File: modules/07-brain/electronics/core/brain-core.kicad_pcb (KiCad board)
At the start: 2 copper layers, 60.5 x 110 mm, 104 parts, among them J1 Conn_02x03_Odd_Even, J10 Conn_01x02, J11 Conn_01x01, J13 Conn_01x03, J2 Conn_02x02_Odd_Even, J3 Conn_02x02_Odd_Even, J4 Conn_02x03_Odd_Even, J5 Conn_01x02, J6 Conn_02x05_Odd_Even, J7 Conn_02x05_Odd_Even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

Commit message: Verfied JLCPCB for Brain 1.0
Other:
- board text added: "SHMØERGH MODULEUR"
- board text added: "SM-07 BRAIN V1.0 / 2025 DEC"
- board text removed: "HM-07 Brain V0.1 / 2025 Sept"
- board text removed: "SHMØERGH HOG MODULEUR"

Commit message: Changed Brain J_DEV header to horizontal
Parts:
- removed the G*** at (133.7, 116.0)
- J_DEV1: footprint Connector_PinHeader_2.54mm:PinHeader_1x02_P2.54mm_Vertical -> Connector_PinHeader_2.54mm:PinHeader_1x02_P2.54mm_Horizontal
- moved J_DEV1 2.54 mm to (133.8, 60.5), turned to 90 degrees
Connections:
- J_DEV1 pad 1: /MCU/UART_TX -> /MCU/UART_RX
- J_DEV1 pad 2: /MCU/UART_RX -> /MCU/UART_TX

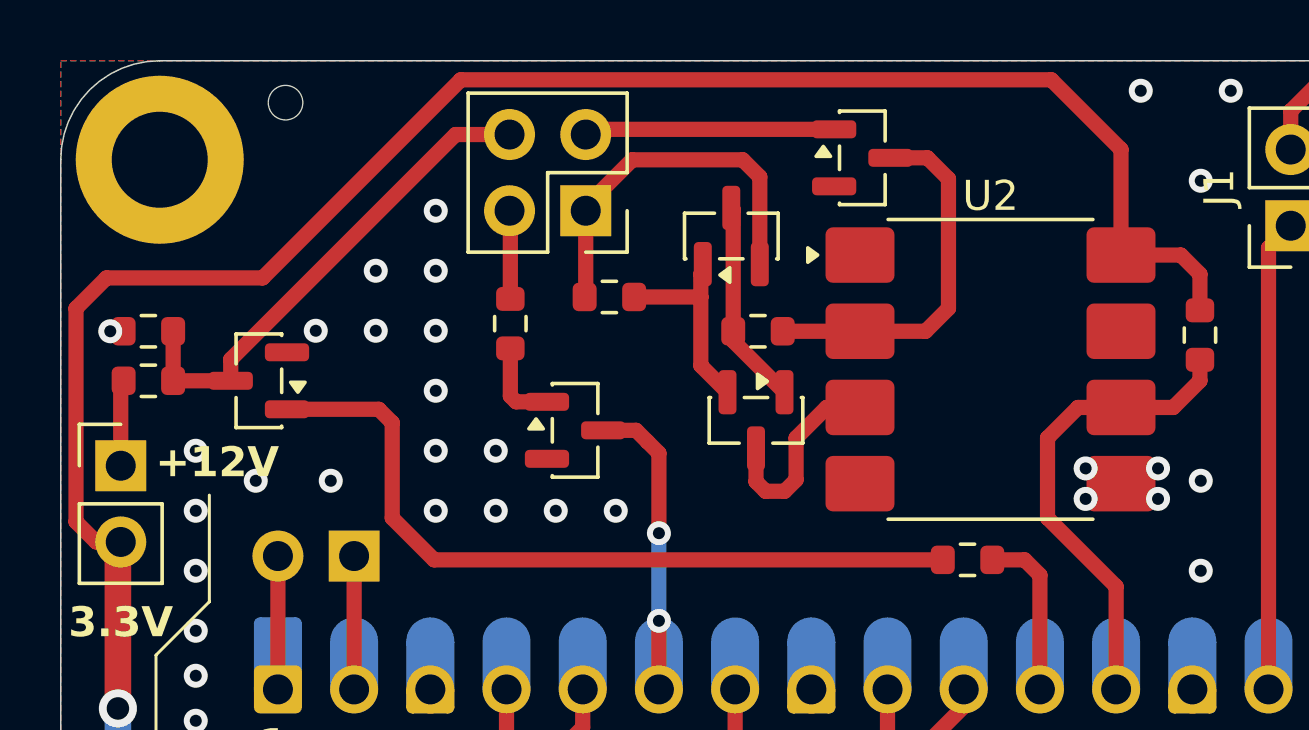
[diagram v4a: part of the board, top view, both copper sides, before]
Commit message: Added protection resistor to pulse out on Brain
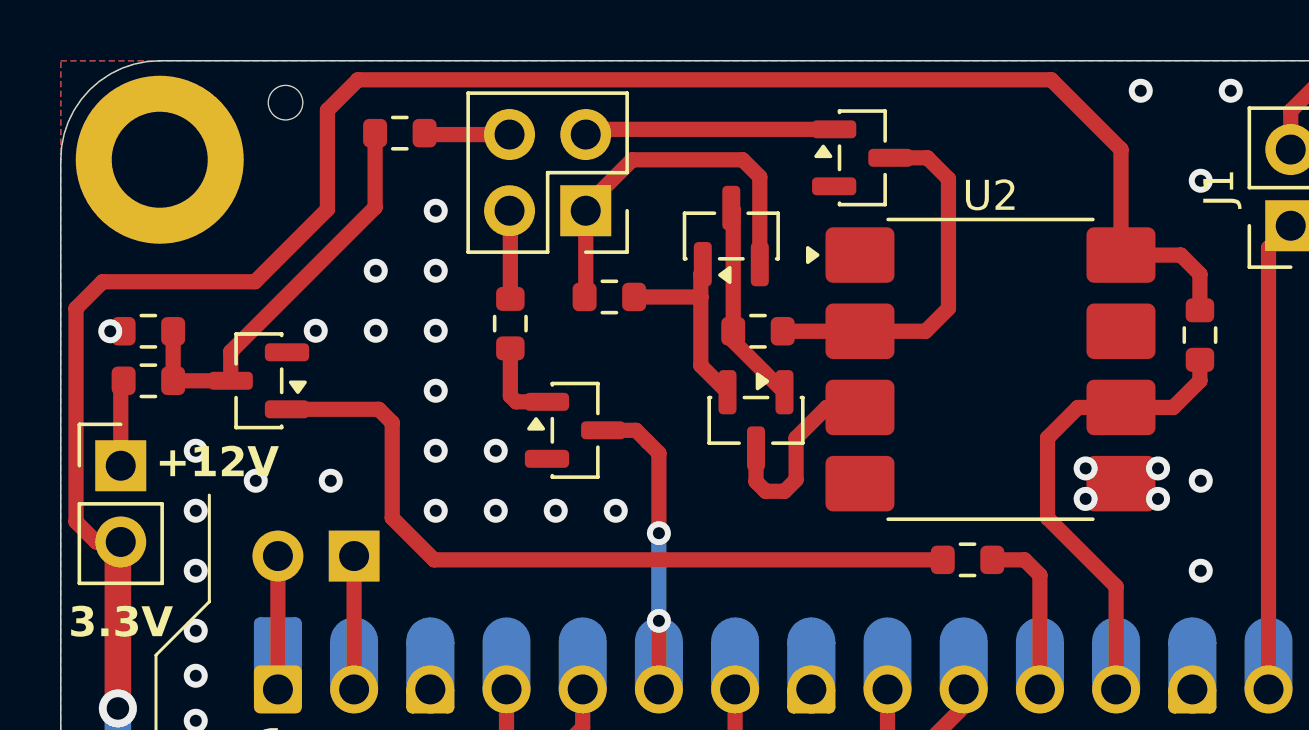
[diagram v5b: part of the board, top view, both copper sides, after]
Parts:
- added R13: 1k, Resistor_SMD:R_0603_1608Metric, F.Cu at (135.3, 46.4)
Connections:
- Q3 pad 3: PULSE_OUT -> Net-(Q3-C)
- R3 pad 1: PULSE_OUT -> Net-(Q3-C)
- R4 pad 2: PULSE_OUT -> Net-(Q3-C)
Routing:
- net PULSE_OUT: track 16.7 -> 2.85 mm
- net Net-(Q3-C): track 0.00 -> 13.8 mm
- net +3.3V: track 155.3 -> 157.2 mm

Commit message: KiCAD version update - Brain
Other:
- board text added: "SM-07 BRAIN V1.1"
- board text removed: "SM-07 BRAIN V1.0 / 2025 DEC"
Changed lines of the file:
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@@
 		)
 	)
-	(gr_text "SM-07 \nBRAIN\nV1.0 / 2025 DEC"
+	(gr_text "SM-07 \nBRAIN\nV1.1"
 		(at 148.384 122.354 0)
 		(layer "B.SilkS")
@@
 			(justify left bottom mirror)
 		)
-		(render_cache "SM-07 \nBRAIN\nV1.0 / 2025 DEC" 0
+		(render_cache "SM-07 \nBRAIN\nV1.1" 0
 			(polygon
 				(pts
@@
 			(polygon
 				(pts
-					(xy 145.167089 121.129498) (xy 145.167089 122.012161) (xy 145.016257 122.012161) (xy 145.016257 121.719415)
-					(xy 144.869849 121.719415) (xy 144.869849 121.568583) (xy 145.016257 121.568583) (xy 145.016257 121.129498)
-				)
-			)
-			(polygon
-				(pts
-					(xy 145.020751 122.007667) (xy 145.020751 122.1585) (xy 144.577172 122.1585) (xy 144.577172 122.007667)
-				)
-			)
-			(polygon
-				(pts
-					(xy 145.020751 120.98309) (xy 145.020751 121.133992) (xy 144.577172 121.133992) (xy 144.577172 120.98309)
-				)
-			)
-			(polygon
-				(pts
-					(xy 144.581667 121.129498) (xy 144.581667 121.275836) (xy 144.728005 121.275836) (xy 144.728005 121.426739)
-					(xy 144.581667 121.426739) (xy 144.581667 122.012161) (xy 144.430764 122.012161) (xy 144.430764 121.129498)
-				)
-			)
-			(polygon
-				(pts
-					(xy 144.874343 121.422245) (xy 144.874343 121.573077) (xy 144.723511 121.573077) (xy 144.723511 121.422245)
-				)
-			)
-			(polygon
-				(pts
-					(xy 142.680956 121.129498) (xy 142.680956 121.426739) (xy 142.530124 121.426739) (xy 142.530124 121.129498)
-				)
-			)
-			(polygon
-				(pts
-					(xy 143.120041 122.007667) (xy 143.120041 122.304908) (xy 142.969209 122.304908) (xy 142.969209 122.007667)
-				)
-			)
-			(polygon
-				(pts
-					(xy 142.973703 121.714921) (xy 142.973703 122.012161) (xy 142.822801 122.012161) (xy 142.822801 121.714921)
-				)
-			)
-			(polygon
-				(pts
-					(xy 142.827295 121.422245) (xy 142.827295 121.719415) (xy 142.676462 121.719415) (xy 142.676462 121.422245)
-				)
-			)
-			(polygon
-				(pts
-					(xy 142.534618 120.836752) (xy 142.534618 121.133992) (xy 142.383716 121.133992) (xy 142.383716 120.836752)
-				)
-			)
-			(polygon
-				(pts
-					(xy 141.072993 121.861329) (xy 141.072993 122.1585) (xy 140.336668 122.1585) (xy 140.336668 122.007667)
-					(xy 140.922161 122.007667) (xy 140.922161 121.861329)
-				)
-			)
-			(polygon
-				(pts
-					(xy 140.483076 121.133992) (xy 140.483076 120.98309) (xy 140.926655 120.98309) (xy 140.926655 121.133992)
-				)
-			)
-			(polygon
-				(pts
-					(xy 140.48757 121.129498) (xy 140.48757 121.426739) (xy 140.336668 121.426739) (xy 140.336668 121.129498)
-				)
-			)
-			(polygon
-				(pts
-					(xy 140.926655 121.714921) (xy 140.926655 121.865823) (xy 140.775752 121.865823) (xy 140.775752 121.714921)
-				)
-			)
-			(polygon
-				(pts
-					(xy 141.072993 121.129498) (xy 141.072993 121.28033) (xy 140.922161 121.28033) (xy 140.922161 121.129498)
-				)
-			)
-			(polygon
-				(pts
-					(xy 140.633908 121.422245) (xy 140.633908 121.573077) (xy 140.483076 121.573077) (xy 140.483076 121.422245)
-				)
-			)
-			(polygon
-				(pts
-					(xy 140.780246 121.568583) (xy 140.780246 121.719415) (xy 140.629414 121.719415) (xy 140.629414 121.568583)
-				)
-			)
-			(polygon
-				(pts
-					(xy 140.049469 121.129498) (xy 140.049469 122.012161) (xy 139.898637 122.012161) (xy 139.898637 121.719415)
-					(xy 139.752228 121.719415) (xy 139.752228 121.568583) (xy 139.898637 121.568583) (xy 139.898637 121.129498)
-				)
-			)
-			(polygon
-				(pts
-					(xy 139.903131 122.007667) (xy 139.903131 122.1585) (xy 139.459552 122.1585) (xy 139.459552 122.007667)
-				)
-			)
-			(polygon
-				(pts
-					(xy 139.903131 120.98309) (xy 139.903131 121.133992) (xy 139.459552 121.133992) (xy 139.459552 120.98309)
-				)
-			)
-			(polygon
-				(pts
-					(xy 139.464046 121.129498) (xy 139.464046 121.275836) (xy 139.610384 121.275836) (xy 139.610384 121.426739)
-					(xy 139.464046 121.426739) (xy 139.464046 122.012161) (xy 139.313144 122.012161) (xy 139.313144 121.129498)
-				)
-			)
-			(polygon
-				(pts
-					(xy 139.756722 121.422245) (xy 139.756722 121.573077) (xy 139.60589 121.573077) (xy 139.60589 121.422245)
-				)
-			)
-			(polygon
-				(pts
-					(xy 139.025945 121.861329) (xy 139.025945 122.1585) (xy 138.28962 122.1585) (xy 138.28962 122.007667)
-					(xy 138.875113 122.007667) (xy 138.875113 121.861329)
-				)
-			)
-			(polygon
-				(pts
-					(xy 138.436028 121.133992) (xy 138.436028 120.98309) (xy 138.879607 120.98309) (xy 138.879607 121.133992)
-				)
-			)
-			(polygon
-				(pts
-					(xy 138.440522 121.129498) (xy 138.440522 121.426739) (xy 138.28962 121.426739) (xy 138.28962 121.129498)
-				)
-			)
-			(polygon
-				(pts
-					(xy 138.879607 121.714921) (xy 138.879607 121.865823) (xy 138.728704 121.865823) (xy 138.728704 121.714921)
-				)
-			)
-			(polygon
-				(pts
-					(xy 139.025945 121.129498) (xy 139.025945 121.28033) (xy 138.875113 121.28033) (xy 138.875113 121.129498)
-				)
-			)
-			(polygon
-				(pts
-					(xy 138.58686 121.422245) (xy 138.58686 121.573077) (xy 138.436028 121.573077) (xy 138.436028 121.422245)
-				)
-			)
-			(polygon
-				(pts
-					(xy 138.733198 121.568583) (xy 138.733198 121.719415) (xy 138.582366 121.719415) (xy 138.582366 121.568583)
-				)
-			)
-			(polygon
-				(pts
-					(xy 138.002421 120.98309) (xy 138.002421 121.573077) (xy 137.412504 121.573077) (xy 137.412504 121.422245)
-					(xy 137.851588 121.422245) (xy 137.851588 121.133992) (xy 137.266096 121.133992) (xy 137.266096 120.98309)
-				)
-			)
-			(polygon
-				(pts
-					(xy 137.416998 121.568583) (xy 137.416998 122.012161) (xy 137.266096 122.012161) (xy 137.266096 121.568583)
-				)
-			)
-			(polygon
-				(pts
-					(xy 137.412504 122.007667) (xy 137.856083 122.007667) (xy 137.856083 122.1585) (xy 137.412504 122.1585)
-				)
-			)
-			(polygon
-				(pts
-					(xy 137.851588 122.012161) (xy 137.851588 121.861329) (xy 138.002421 121.861329) (xy 138.002421 122.012161)
-				)
-			)
-			(polygon
-				(pts
-					(xy 135.955372 120.98309) (xy 135.955372 122.1585) (xy 135.365456 122.1585) (xy 135.365456 122.007667)
-					(xy 135.80454 122.007667) (xy 135.80454 121.133992) (xy 135.365456 121.133992) (xy 135.365456 120.98309)
-				)
-			)
-			(polygon
-				(pts
-					(xy 135.36995 121.129498) (xy 135.36995 122.012161) (xy 135.219047 122.012161) (xy 135.219047 121.129498)
-				)
-			)
-			(polygon
-				(pts
-					(xy 134.931848 120.98309) (xy 134.931848 122.1585) (xy 134.195523 122.1585) (xy 134.195523 122.007667)
-					(xy 134.781016 122.007667) (xy 134.781016 121.573077) (xy 134.341932 121.573077) (xy 134.341932 121.422245)
-					(xy 134.781016 121.422245) (xy 134.781016 121.133992) (xy 134.195523 121.133992) (xy 134.195523 120.98309)
-				)
-			)
-			(polygon
-				(pts
-					(xy 133.908324 121.129498) (xy 133.908324 122.012161) (xy 133.757492 122.012161) (xy 133.757492 121.129498)
-				)
-			)
-			(polygon
-				(pts
-					(xy 133.761986 122.007667) (xy 133.761986 122.1585) (xy 133.318408 122.1585) (xy 133.318408 122.007667)
-				)
-			)
-			(polygon
-				(pts
-					(xy 133.322902 121.861329) (xy 133.322902 122.012161) (xy 133.171999 122.012161) (xy 133.171999 121.861329)
-				)
-			)
-			(polygon
-				(pts
-					(xy 133.761986 120.98309) (xy 133.761986 121.133992) (xy 133.318408 121.133992) (xy 133.318408 120.98309)
-				)
-			)
-			(polygon
-				(pts
-					(xy 133.322902 121.129498) (xy 133.322902 121.28033) (xy 133.171999 121.28033) (xy 133.171999 121.129498)
-				)
-			)
+					(xy 144.874343 121.28033) (xy 144.874343 122.007667) (xy 145.167089 122.007667) (xy 145.167089 122.1585)
+					(xy 144.430764 122.1585) (xy 144.430764 122.007667) (xy 144.723511 122.007667) (xy 144.723511 120.98309)
+					(xy 144.874343 120.98309) (xy 144.874343 121.129498) (xy 145.167089 121.129498) (xy 145.167089 121.28033)
+				)
+			)

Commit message: Updated rev. number in Brain
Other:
- board text added: "SM-07 BRAIN V1.2"
- board text removed: "SM-07 BRAIN V1.1"
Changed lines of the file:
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@@
 		)
 	)
-	(gr_text "SM-07 \nBRAIN\nV1.1"
+	(gr_text "SM-07 \nBRAIN\nV1.2"
 		(at 148.384 122.354 0)
 		(layer "B.SilkS")
@@
 			(justify left bottom mirror)
 		)
-		(render_cache "SM-07 \nBRAIN\nV1.1" 0
+		(render_cache "SM-07 \nBRAIN\nV1.2" 0
 			(polygon
 				(pts
@@
 			(polygon
 				(pts
-					(xy 144.874343 121.28033) (xy 144.874343 122.007667) (xy 145.167089 122.007667) (xy 145.167089 122.1585)
-					(xy 144.430764 122.1585) (xy 144.430764 122.007667) (xy 144.723511 122.007667) (xy 144.723511 120.98309)
-					(xy 144.874343 120.98309) (xy 144.874343 121.129498) (xy 145.167089 121.129498) (xy 145.167089 121.28033)
-				)
-			)
+					(xy 145.167089 121.861329) (xy 145.167089 122.1585) (xy 144.430764 122.1585) (xy 144.430764 122.007667)
+					(xy 145.016257 122.007667) (xy 145.016257 121.861329)
+				)
+			)
+			(polygon
+				(pts
+					(xy 144.577172 121.133992) (xy 144.577172 120.98309) (xy 145.020751 120.98309) (xy 145.020751 121.133992)
+				)
+			)
+			(polygon
+				(pts
+					(xy 144.581667 121.129498) (xy 144.581667 121.426739) (xy 144.430764 121.426739) (xy 144.430764 121.129498)
+				)
+			)
+			(polygon
+				(pts
+					(xy 145.020751 121.714921) (xy 145.020751 121.865823) (xy 144.869849 121.865823) (xy 144.869849 121.714921)
+				)
+			)
+			(polygon
+				(pts
+					(xy 145.167089 121.129498) (xy 145.167089 121.28033) (xy 145.016257 121.28033) (xy 145.016257 121.129498)
+				)
+			)
+			(polygon
+				(pts
+					(xy 144.728005 121.422245) (xy 144.728005 121.573077) (xy 144.577172 121.573077) (xy 144.577172 121.422245)
+				)
+			)
+			(polygon
+				(pts
+					(xy 144.874343 121.568583) (xy 144.874343 121.719415) (xy 144.723511 121.719415) (xy 144.723511 121.568583)
+				)
+			)
